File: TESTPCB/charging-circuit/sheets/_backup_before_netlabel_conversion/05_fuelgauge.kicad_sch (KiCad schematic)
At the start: 2 parts, among them P2 Header-Male-2.54_2x2, U1 MAX17048G+T10

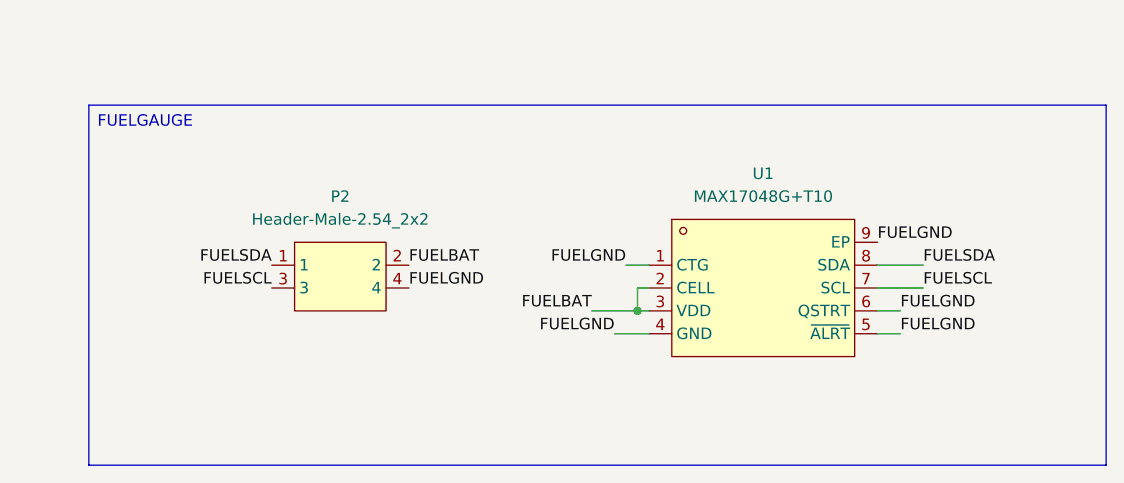
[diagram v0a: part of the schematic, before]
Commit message: Fixed formatting issues, now the hierachal sheets are all labeled as net labels and when we want to expose their pins we will make them into hierchal or global pins
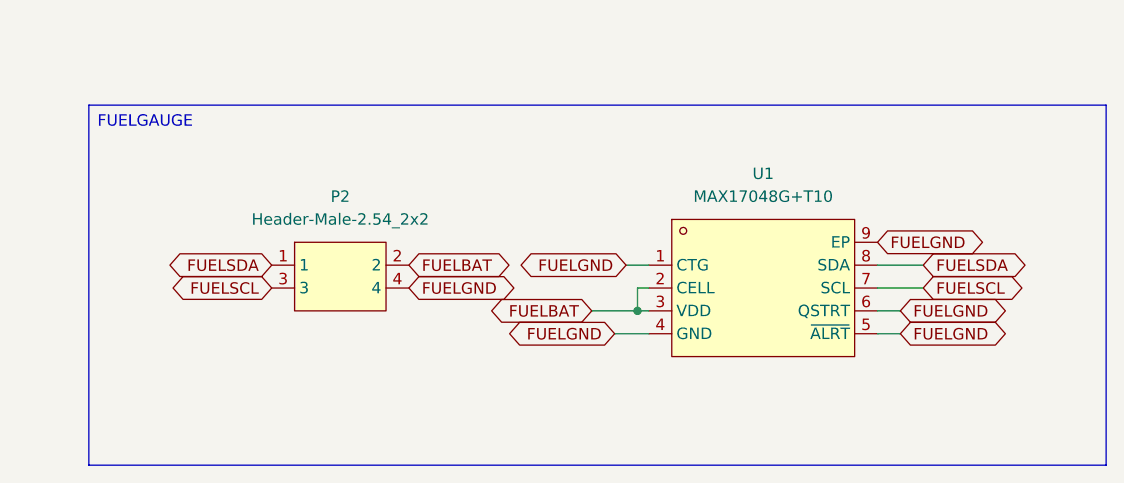
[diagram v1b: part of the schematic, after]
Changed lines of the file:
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@@
 		)
 	)
-	(label "FUELGND"
+	(global_label "FUELGND"
+		(shape bidirectional)
 		(at 173.99 88.9 0)
 		(effects
@@
 			(justify left bottom)
 		)
-	)
-	(label "FUELGND"
+		(property "Intersheetrefs" "${INTERSHEET_REFS}"
+			(at 173.99 88.9 0)
+			(effects
+				(font
+					(size 1.27 1.27)
+				)
+				(hide yes)
+			)
+		)
+	)
+	(global_label "FUELGND"
+		(shape bidirectional)
 		(at 119.38 83.82 0)
 		(effects
@@
 			(justify left bottom)
 		)
-	)
-	(label "FUELBAT"
+		(property "Intersheetrefs" "${INTERSHEET_REFS}"
+			(at 119.38 83.82 0)
+			(effects
+				(font
+					(size 1.27 1.27)
+				)
+				(hide yes)
+			)
+		)
+	)
+	(global_label "FUELBAT"
+		(shape bidirectional)
 		(at 139.7 86.36 180)
 		(effects
@@
 			(justify right bottom)
 		)
-	)
-	(label "FUELGND"
+		(property "Intersheetrefs" "${INTERSHEET_REFS}"
+			(at 139.7 86.36 0)
+			(effects
+				(font
+					(size 1.27 1.27)
+				)
+				(hide yes)
+			)
+		)
+	)
+	(global_label "FUELGND"
+		(shape bidirectional)
 		(at 173.99 86.36 0)
 		(effects
@@
 			(justify left bottom)
 		)
-	)
-	(label "FUELGND"
+		(property "Intersheetrefs" "${INTERSHEET_REFS}"
+			(at 173.99 86.36 0)
+			(effects
+				(font
+					(size 1.27 1.27)
+				)
+				(hide yes)
+			)
+		)
+	)
+	(global_label "FUELGND"
+		(shape bidirectional)
 		(at 142.24 88.9 180)
 		(effects
@@
 			(justify right bottom)
 		)
-	)
-	(label "FUELBAT"
+		(property "Intersheetrefs" "${INTERSHEET_REFS}"
+			(at 142.24 88.9 0)
+			(effects
+				(font
+					(size 1.27 1.27)
+				)
+				(hide yes)
+			)
+		)
+	)
+	(global_label "FUELBAT"
+		(shape bidirectional)
 		(at 119.38 81.28 0)
 		(effects
@@
 			(justify left bottom)
 		)
-	)
-	(label "FUELGND"
+		(property "Intersheetrefs" "${INTERSHEET_REFS}"
+			(at 119.38 81.28 0)
+			(effects
+				(font
+					(size 1.27 1.27)
+				)
+				(hide yes)
+			)
+		)
+	)
+	(global_label "FUELGND"
+		(shape bidirectional)
 		(at 171.45 78.74 0)
 		(effects
@@
 			(justify left bottom)
 		)
-	)
-	(label "FUELSDA"
+		(property "Intersheetrefs" "${INTERSHEET_REFS}"
+			(at 171.45 78.74 0)
+			(effects
+				(font
+					(size 1.27 1.27)
+				)
+				(hide yes)
+			)
+		)
+	)
+	(global_label "FUELSDA"
+		(shape bidirectional)
 		(at 176.53 81.28 0)
 		(effects
@@
 			(justify left bottom)
 		)
-	)
-	(label "FUELGND"
+		(property "Intersheetrefs" "${INTERSHEET_REFS}"
+			(at 176.53 81.28 0)
+			(effects
+				(font
+					(size 1.27 1.27)
+				)
+				(hide yes)
+			)
+		)
+	)
+	(global_label "FUELGND"
+		(shape bidirectional)
 		(at 143.51 81.28 180)
 		(effects
@@
 			(justify right bottom)
 		)
-	)
-	(label "FUELSDA"
+		(property "Intersheetrefs" "${INTERSHEET_REFS}"
+			(at 143.51 81.28 0)
+			(effects
+				(font
+					(size 1.27 1.27)
+				)
+				(hide yes)
+			)
+		)
+	)
+	(global_label "FUELSDA"
+		(shape bidirectional)
 		(at 104.14 81.28 180)
 		(effects
@@
 			(justify right bottom)
 		)
-	)
-	(label "FUELSCL"
+		(property "Intersheetrefs" "${INTERSHEET_REFS}"
+			(at 104.14 81.28 0)
+			(effects
+				(font
+					(size 1.27 1.27)
+				)
+				(hide yes)
+			)
+		)
+	)
+	(global_label "FUELSCL"
+		(shape bidirectional)
 		(at 176.53 83.82 0)
 		(effects
@@
 			(justify left bottom)
 		)
-	)
-	(label "FUELSCL"
+		(property "Intersheetrefs" "${INTERSHEET_REFS}"
+			(at 176.53 83.82 0)
+			(effects
+				(font
+					(size 1.27 1.27)
+				)
+				(hide yes)
+			)
+		)
+	)
+	(global_label "FUELSCL"
+		(shape bidirectional)
 		(at 104.14 83.82 180)
 		(effects
@@
 			(justify right bottom)
 		)
-	)
+		(property "Intersheetrefs" "${INTERSHEET_REFS}"
+			(at 104.14 83.82 0)
+			(effects
+				(font
+					(size 1.27 1.27)
+				)
+				(hide yes)
+			)
+		)
+	)
